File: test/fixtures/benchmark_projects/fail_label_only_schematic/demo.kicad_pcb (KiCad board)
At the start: 25 x 20 mm, 0 parts

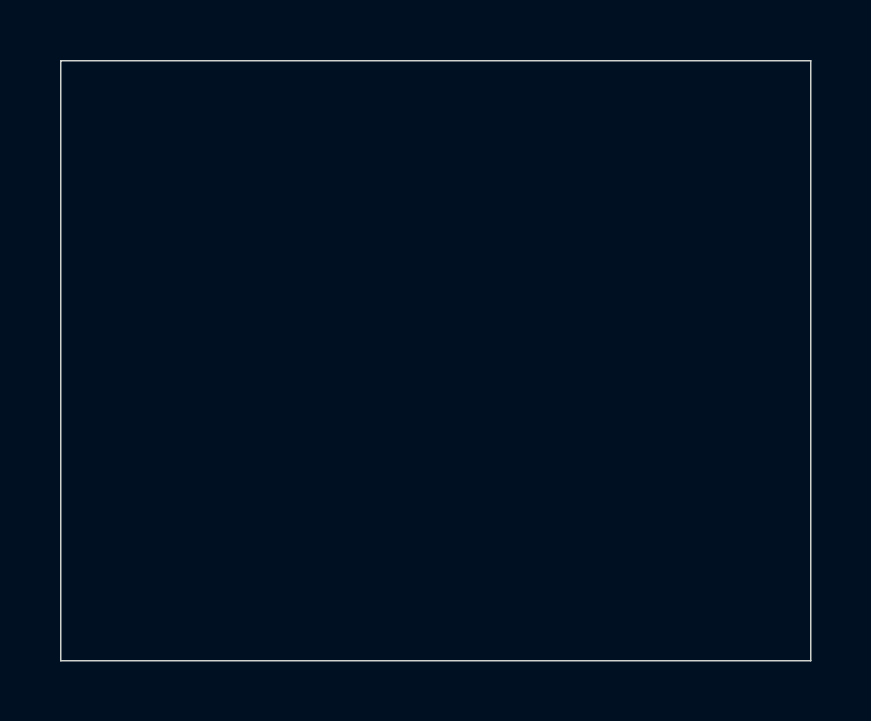
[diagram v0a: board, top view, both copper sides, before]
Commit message: test(fixtures): clean up and fix benchmark project fixtures
- Remove 4 empty kicad10_* stub projects (kicad10_variants,
  kicad10_timedomain, kicad10_custom_drc, kicad10_design_blocks)
  that had no schematic/PCB content and were not referenced by any test
- Remove stray demo.kicad_prl from fail_bad_decoupling_placement
- Fix 3 fail_* projects whose schematics were empty while PCBs had
  content (fail_bad_decoupling_placement, fail_dfm_edge_clearance,
  fail_sensor_cluster_spread): add matching component symbols
- Fix 3 fail_* projects whose PCBs were empty while schematics had
  content (fail_label_only_schematic, fail_sismosmart_like_hierarchy,
  fail_sismosmart_like_label_only): add matching footprints

All 10 remaining fixtures now have consistent schematic + PCB content
that matches their intended failure scenario.
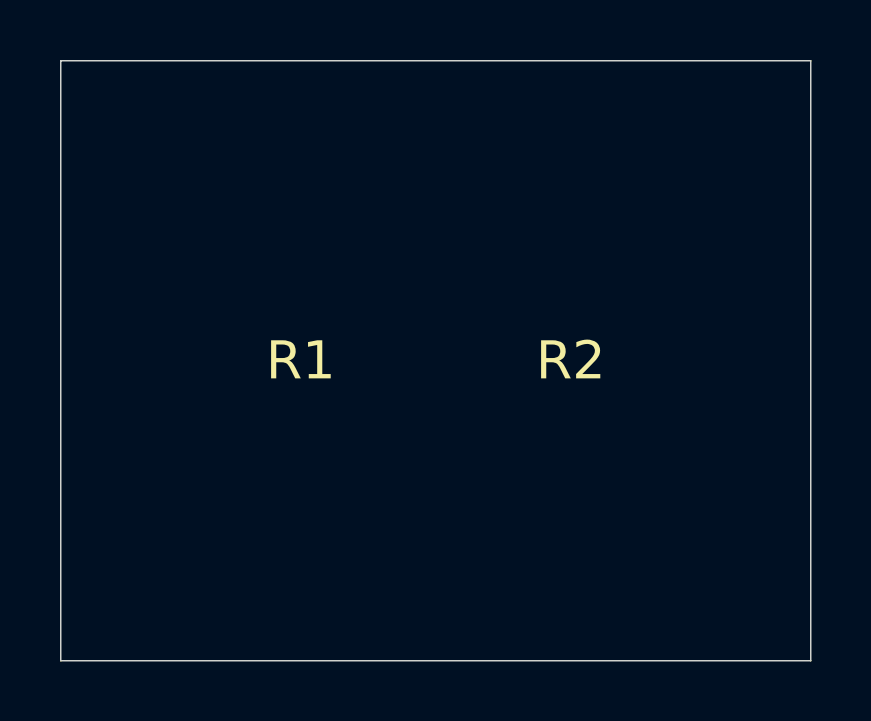
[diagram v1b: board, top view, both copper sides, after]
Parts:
- added R1: 10k, Resistor_SMD:R_0805, F.Cu at (8.00, 10.0)
- added R2: 22k, Resistor_SMD:R_0805, F.Cu at (17.0, 10.0)
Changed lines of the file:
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@@
   (generator "pytest")
   (gr_rect (start 0 0) (end 25 20) (stroke (width 0.05) (type solid)) (fill no) (layer "Edge.Cuts"))
+  (footprint "Resistor_SMD:R_0805"
+    (layer "F.Cu")
+    (at 8 10 0)
+    (property "Reference" "R1" (at 0 0 0) (layer "F.SilkS"))
+    (property "Value" "10k" (at 0 1.5 0) (layer "F.Fab"))
+    (fp_rect (start -1.5 -0.8) (end 1.5 0.8) (stroke (width 0.05) (type solid)) (fill no) (layer "F.CrtYd"))
+  )
+  (footprint "Resistor_SMD:R_0805"
+    (layer "F.Cu")
+    (at 17 10 0)
+    (property "Reference" "R2" (at 0 0 0) (layer "F.SilkS"))
+    (property "Value" "22k" (at 0 1.5 0) (layer "F.Fab"))
+    (fp_rect (start -1.5 -0.8) (end 1.5 0.8) (stroke (width 0.05) (type solid)) (fill no) (layer "F.CrtYd"))
+  )
 )
